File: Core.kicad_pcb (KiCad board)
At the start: 2 copper layers, 88 x 88 mm, 5 parts, among them J1 GPIO

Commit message: Test 3 - Change circuit
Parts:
- J1: value GPIO -> Conn_02x20_Odd_Even
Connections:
- J1 pad 1: (no net) -> unconnected-(J1-Pin_1-Pad1)
- J1 pad 10: (no net) -> unconnected-(J1-Pin_10-Pad10)
- J1 pad 11: (no net) -> unconnected-(J1-Pin_11-Pad11)
- J1 pad 12: (no net) -> unconnected-(J1-Pin_12-Pad12)
- J1 pad 13: (no net) -> unconnected-(J1-Pin_13-Pad13)
- J1 pad 14: (no net) -> unconnected-(J1-Pin_14-Pad14)
- J1 pad 15: (no net) -> unconnected-(J1-Pin_15-Pad15)
- J1 pad 16: (no net) -> unconnected-(J1-Pin_16-Pad16)
- J1 pad 17: (no net) -> unconnected-(J1-Pin_17-Pad17)
- J1 pad 18: (no net) -> unconnected-(J1-Pin_18-Pad18)
- J1 pad 19: (no net) -> unconnected-(J1-Pin_19-Pad19)
- J1 pad 2: (no net) -> unconnected-(J1-Pin_2-Pad2)
- J1 pad 20: (no net) -> unconnected-(J1-Pin_20-Pad20)
- J1 pad 21: (no net) -> unconnected-(J1-Pin_21-Pad21)
- J1 pad 22: (no net) -> unconnected-(J1-Pin_22-Pad22)
- J1 pad 23: (no net) -> unconnected-(J1-Pin_23-Pad23)
- J1 pad 24: (no net) -> unconnected-(J1-Pin_24-Pad24)
- J1 pad 25: (no net) -> unconnected-(J1-Pin_25-Pad25)
- J1 pad 26: (no net) -> unconnected-(J1-Pin_26-Pad26)
- J1 pad 27: (no net) -> unconnected-(J1-Pin_27-Pad27)
- J1 pad 28: (no net) -> unconnected-(J1-Pin_28-Pad28)
- J1 pad 29: (no net) -> unconnected-(J1-Pin_29-Pad29)
- J1 pad 3: (no net) -> unconnected-(J1-Pin_3-Pad3)
- J1 pad 30: (no net) -> unconnected-(J1-Pin_30-Pad30)
- J1 pad 31: (no net) -> unconnected-(J1-Pin_31-Pad31)
- J1 pad 32: (no net) -> unconnected-(J1-Pin_32-Pad32)
- J1 pad 33: (no net) -> unconnected-(J1-Pin_33-Pad33)
- J1 pad 34: (no net) -> unconnected-(J1-Pin_34-Pad34)
- J1 pad 35: (no net) -> unconnected-(J1-Pin_35-Pad35)
- J1 pad 36: (no net) -> unconnected-(J1-Pin_36-Pad36)
- J1 pad 37: (no net) -> unconnected-(J1-Pin_37-Pad37)
- J1 pad 38: (no net) -> unconnected-(J1-Pin_38-Pad38)
- J1 pad 39: (no net) -> unconnected-(J1-Pin_39-Pad39)
- J1 pad 4: (no net) -> unconnected-(J1-Pin_4-Pad4)
- J1 pad 40: (no net) -> unconnected-(J1-Pin_40-Pad40)
- J1 pad 5: (no net) -> unconnected-(J1-Pin_5-Pad5)
- J1 pad 6: (no net) -> unconnected-(J1-Pin_6-Pad6)
- J1 pad 7: (no net) -> unconnected-(J1-Pin_7-Pad7)
- J1 pad 8: (no net) -> unconnected-(J1-Pin_8-Pad8)
- J1 pad 9: (no net) -> unconnected-(J1-Pin_9-Pad9)

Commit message: Add Power Plane
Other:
- copper layers 2 -> 4
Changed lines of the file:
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@@
 	(generator_version "8.0")
 	(general
-		(thickness 1.600198)
+		(thickness 1.6)
 		(legacy_teardrops no)
 	)
 	(paper "A4")
 	(layers
-		(0 "F.Cu" signal "Front")
-		(31 "B.Cu" signal "Back")
+		(0 "F.Cu" signal)
+		(1 "In1.Cu" power "GND.Cu")
+		(2 "In2.Cu" power "Power.Cu")
+		(31 "B.Cu" signal)
+		(32 "B.Adhes" user "B.Adhesive")
+		(33 "F.Adhes" user "F.Adhesive")
 		(34 "B.Paste" user)
 		(35 "F.Paste" user)
@@
 		(38 "B.Mask" user)
 		(39 "F.Mask" user)
+		(40 "Dwgs.User" user "User.Drawings")
+		(41 "Cmts.User" user "User.Comments")
+		(42 "Eco1.User" user "User.Eco1")
+		(43 "Eco2.User" user "User.Eco2")
 		(44 "Edge.Cuts" user)
 		(45 "Margin" user)
 		(46 "B.CrtYd" user "B.Courtyard")
 		(47 "F.CrtYd" user "F.Courtyard")
+		(48 "B.Fab" user)
 		(49 "F.Fab" user)
 	)
@@
 			(layer "dielectric 1"
 				(type "core")
-				(thickness 1.510198)
+				(thickness 0.48)
 				(material "FR4")
 				(epsilon_r 4.5)
+				(loss_tangent 0.02)
+			)
+			(layer "In1.Cu"
+				(type "copper")
+				(thickness 0.035)
+			)
+			(layer "dielectric 2"
+				(type "prepreg")
+				(thickness 0.48)
+				(material "FR4")
+				(epsilon_r 4.5)
+				(loss_tangent 0.02)
+			)
+			(layer "In2.Cu"
+				(type "copper")
+				(thickness 0.035)
+			)
+			(layer "dielectric 3"
+				(type "core")
+				(thickness 0.48)
+				(material "FR4")
+				(epsilon_r 4.5)

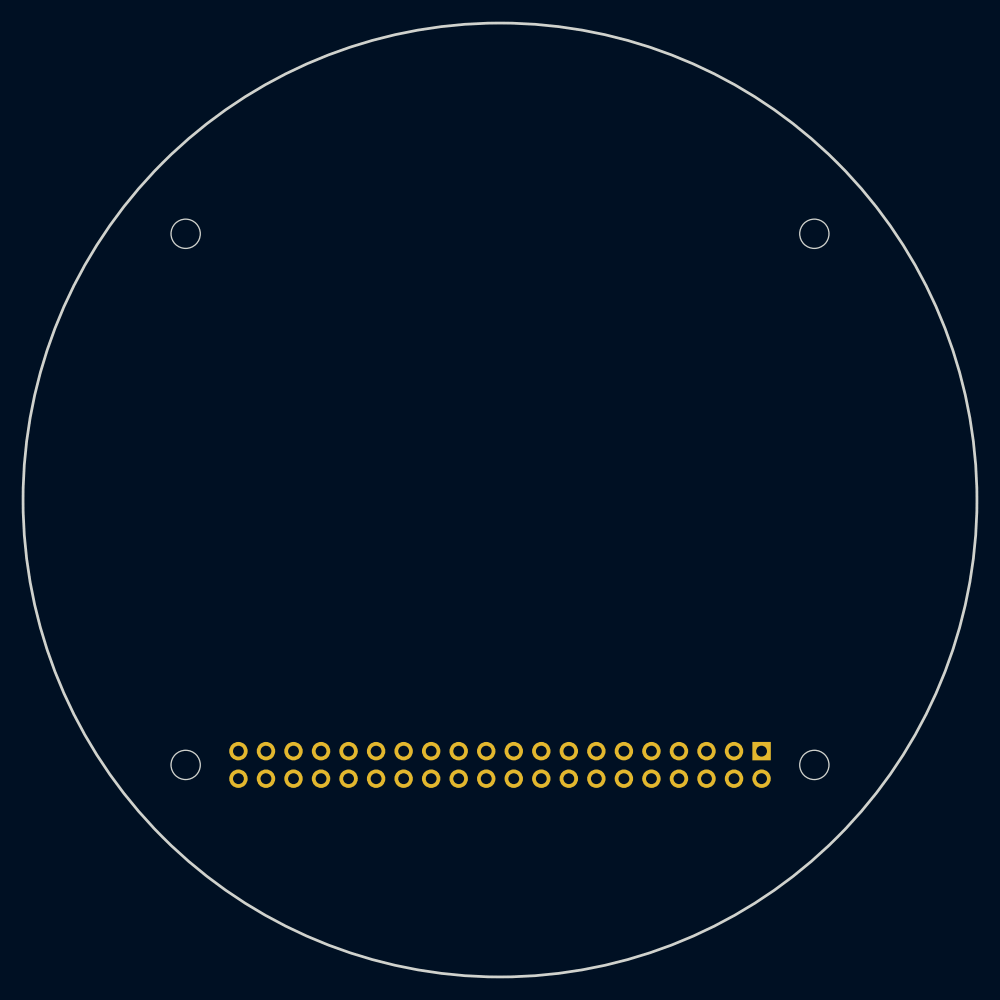
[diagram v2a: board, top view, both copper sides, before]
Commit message: DRC Fix for mounting holes
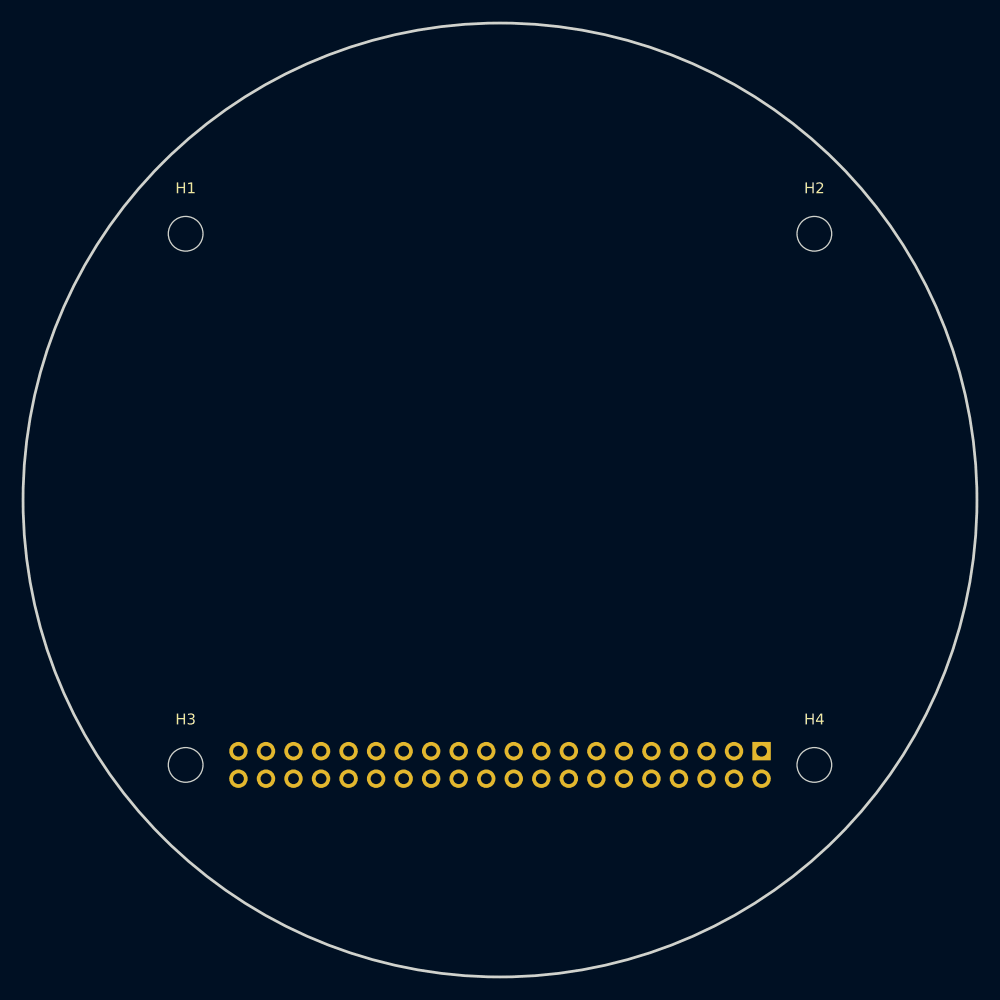
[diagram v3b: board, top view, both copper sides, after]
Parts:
- removed MH1, MH2, MH3, MH4: MountingHole_2.7mm_M2.5, MountingHole:MountingHole_2.7mm_M2.5
- added H1: MountingHole, MountingHole:MountingHole_3.2mm_M3, F.Cu at (41.0, 45.4)
- added H2: MountingHole, MountingHole:MountingHole_3.2mm_M3, F.Cu at (99.0, 45.4)
- added H3: MountingHole, MountingHole:MountingHole_3.2mm_M3, F.Cu at (41.0, 94.4)
- added H4: MountingHole, MountingHole:MountingHole_3.2mm_M3, F.Cu at (99.0, 94.4)
